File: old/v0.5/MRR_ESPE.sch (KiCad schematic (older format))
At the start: 168 parts, among them J1 X_MIN, J10 PART_FAN, J11 UNUSED, J12 T_BED, J13 T_E0, J14 I2C/SPI, J15 AUX1, J16 USB_B_Micro, J17 HS_FAN, J18 CASE_FAN, J19 EXT_FAN, J2 Z_MIN, J20 CS_PINS, J21 X_MOTOR, J22 Z_MOTOR, J23 Y_MOTOR, J24 E0_MOTOR, J25 E1_MOTOR, J26 EXP3, J3 BED, J4 Micro_SD_Card_China, J5 Y_MIN, J6 Z_PROBE, J7 E0, J8 T_EXT, J9 PWR_IN, Q1 IRLS3034PBF, Q2 IRLR8743TRPBF, Q3 WST3392, Q4 S9014, Q5 S9014, Q6 WST3392, SW1 RESET, U1 ESP32-WROOM-32D, U10 TLP182, U11 Pololu_board, U13 74HCT595, U14 74HCT595, U15 74HCT595, U2 TPS54340DDA, U3 CH340C, U4 AMS1117-3.3, U5 Pololu_board, U6 Pololu_board, U7 74HCT595, U8 Pololu_board, U9 Pololu_board

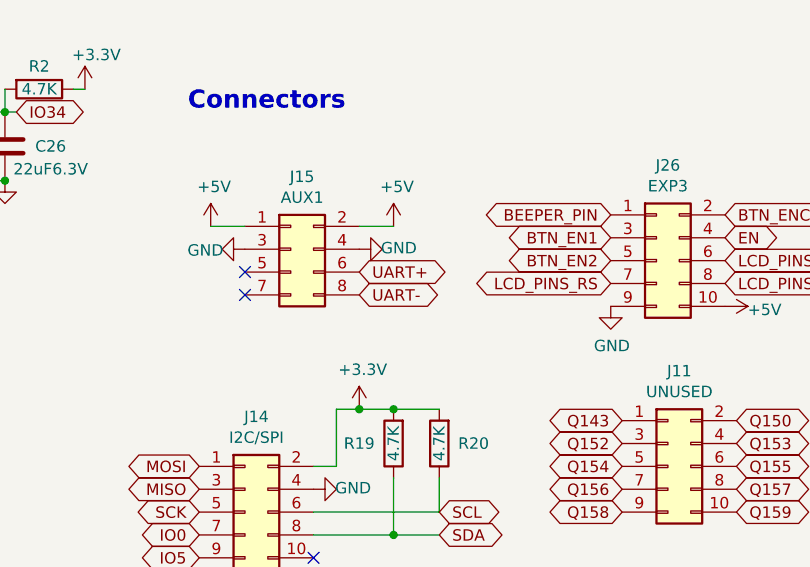
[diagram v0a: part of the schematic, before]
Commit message: Added v0.5rev1 to fix AUX1 issue
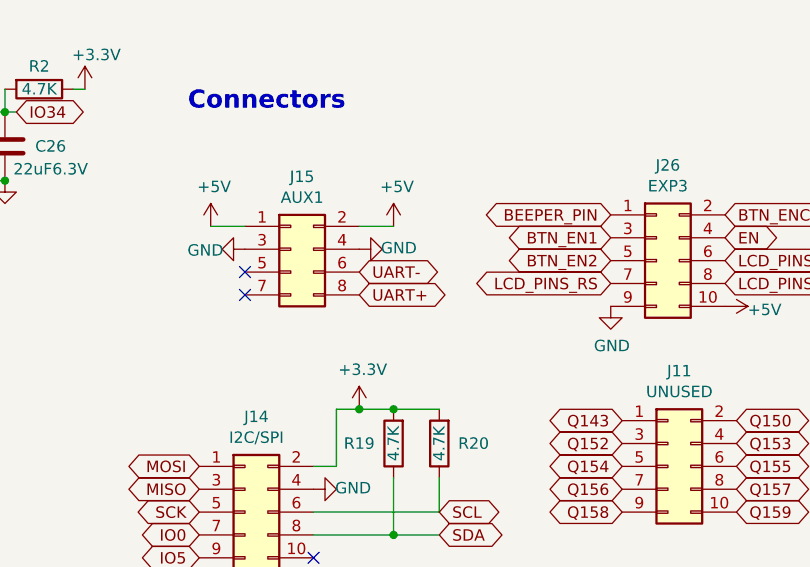
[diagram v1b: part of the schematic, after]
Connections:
- net UART+: now also J15.8 (Pin_8); no longer J15.6 (Pin_6)
- net UART-: now also J15.6 (Pin_6); no longer J15.8 (Pin_8)
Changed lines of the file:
@@
 Sheet 1 1
 Title "MRR ESPE"
-Date "2019-12-09"
-Rev "v0.51"
+Date "2019-10-06"
+Rev "v0.5"
 Comp ""
 Comment1 ""
@@
 	5400 3000 5400 2800
 Connection ~ 5400 2800
-Text GLabel 4750 8750 2    50   BiDi ~ 0
-UART-
 Text GLabel 4750 8650 2    50   BiDi ~ 0
+UART-
+Text GLabel 4750 8750 2    50   BiDi ~ 0
 UART+
 $Comp
